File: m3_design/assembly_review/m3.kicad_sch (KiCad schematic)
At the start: 15 parts, among them J3 USB-C 2.0, U2 AP63203WU-7

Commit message: Validate and harden R5 flight computer CAD
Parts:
- C10, C11, C6, C7, C8, C9: Manufacturer (none) -> Samsung Electro-Mechanics; Manufacturer Part (none) -> CL21A226MAQNNNE
- C28: Manufacturer (none) -> Samsung Electro-Mechanics; Manufacturer Part (none) -> CL10A475KO8NNNC
- C5: Manufacturer (none) -> Samsung Electro-Mechanics; Manufacturer Part (none) -> CL05B104KO5NNNC
- D4: Manufacturer (none) -> STMicroelectronics; Manufacturer Part (none) -> USBLC6-2SC6
- J3: Manufacturer (none) -> Korean Hroparts Elec; Manufacturer Part (none) -> TYPE-C-31-M-12
- L1: Manufacturer (none) -> Sunlord; Manufacturer Part (none) -> SWPA4030S4R7MT
- R164: Manufacturer (none) -> UNI-ROYAL(Uniroyal Elec); Manufacturer Part (none) -> 0603WAF220KT5E
- R7, R8: Manufacturer (none) -> UNI-ROYAL(Uniroyal Elec); Manufacturer Part (none) -> 0402WGF5101TCE
- U2: Manufacturer (none) -> Diodes Incorporated; Manufacturer Part (none) -> AP63203WU-7
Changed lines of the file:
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@@
+				(font
+					(size 1.27 1.27))))
+		(property "Manufacturer" "Korean Hroparts Elec"
+			(at 63.5 76.2 0)
+			(hide yes)
+			(effects
+				(font
+					(size 1.27 1.27))))
+		(property "Manufacturer Part" "TYPE-C-31-M-12"
+			(at 63.5 76.2 0)
+			(hide yes)
+			(effects
 				(font
 					(size 1.27 1.27))))
@@
 				(font
 					(size 1.27 1.27))))
+		(property "Manufacturer" "STMicroelectronics"
+			(at 172.72 76.2 0)
+			(hide yes)
+			(effects
+				(font
+					(size 1.27 1.27))))
+		(property "Manufacturer Part" "USBLC6-2SC6"
+			(at 172.72 76.2 0)
+			(hide yes)
+			(effects
+				(font
+					(size 1.27 1.27))))
 		(instances
 			(project "m3"
@@
 				(font
 					(size 1.27 1.27))))
+		(property "Manufacturer" "Diodes Incorporated"
+			(at 284.48 76.2 0)
+			(hide yes)
+			(effects
+				(font
+					(size 1.27 1.27))))
+		(property "Manufacturer Part" "AP63203WU-7"
+			(at 284.48 76.2 0)
+			(hide yes)
+			(effects
+				(font
+					(size 1.27 1.27))))
 		(instances
 			(project "m3"
@@
 					(size 1.27 1.27))
 				(justify left)))
+		(property "Manufacturer" "Sunlord"
+			(at 261.62 154.94 0)
+			(hide yes)
+			(effects
+				(font
+					(size 1.27 1.27))
+				(justify left)))
+		(property "Manufacturer Part" "SWPA4030S4R7MT"
+			(at 261.62 154.94 0)
+			(hide yes)
+			(effects
+				(font
+					(size 1.27 1.27))
+				(justify left)))
 		(instances
 			(project "m3"
@@
 					(size 1.27 1.27))
 				(justify left)))
+		(property "Manufacturer" "UNI-ROYAL(Uniroyal Elec)"
+			(at 261.62 198.12 0)
+			(hide yes)
+			(effects
+				(font
+					(size 1.27 1.27))
+				(justify left)))
+		(property "Manufacturer Part" "0603WAF220KT5E"
+			(at 261.62 198.12 0)
+			(hide yes)
+			(effects
+				(font
+					(size 1.27 1.27))
+				(justify left)))
 		(instances
 			(project "m3"
@@
 					(size 1.27 1.27))
 				(justify left)))
+		(property "Manufacturer" "UNI-ROYAL(Uniroyal Elec)"
+			(at 40.64 116.84 0)
+			(hide yes)
+			(effects
+				(font
+					(size 1.27 1.27))
+				(justify left)))
+		(property "Manufacturer Part" "0402WGF5101TCE"
+			(at 40.64 116.84 0)
+			(hide yes)
+			(effects
+				(font
+					(size 1.27 1.27))
+				(justify left)))
 		(instances
 			(project "m3"
@@
 					(size 1.27 1.27))
 				(justify left)))
+		(property "Manufacturer" "UNI-ROYAL(Uniroyal Elec)"
+			(at 86.36 116.84 0)
+			(hide yes)
+			(effects
+				(font
+					(size 1.27 1.27))
+				(justify left)))
+		(property "Manufacturer Part" "0402WGF5101TCE"
+			(at 86.36 116.84 0)
+			(hide yes)
+			(effects
+				(font
+					(size 1.27 1.27))
+				(justify left)))
 		(instances
 			(project "m3"
@@
 					(size 1.27 1.27))
 				(justify left)))
+		(property "Manufacturer" "Samsung Electro-Mechanics"
+			(at 248.92 114.3 0)
+			(hide yes)
+			(effects
+				(font
+					(size 1.27 1.27))
+				(justify left)))
+		(property "Manufacturer Part" "CL05B104KO5NNNC"
+			(at 248.92 114.3 0)
+			(hide yes)
+			(effects
+				(font
+					(size 1.27 1.27))
+				(justify left)))
 		(instances
 			(project "m3"
@@
 					(size 1.27 1.27))
 				(justify left)))
+		(property "Manufacturer" "Samsung Electro-Mechanics"
+			(at 279.4 114.3 0)
+			(hide yes)
+			(effects
+				(font
+					(size 1.27 1.27))
+				(justify left)))
+		(property "Manufacturer Part" "CL21A226MAQNNNE"
+			(at 279.4 114.3 0)
+			(hide yes)
+			(effects
+				(font
+					(size 1.27 1.27))
+				(justify left)))
 		(instances
 			(project "m3"
@@
 					(size 1.27 1.27))
 				(justify left)))
+		(property "Manufacturer" "Samsung Electro-Mechanics"
+			(at 309.88 114.3 0)
+			(hide yes)
+			(effects
+				(font
+					(size 1.27 1.27))
+				(justify left)))
+		(property "Manufacturer Part" "CL21A226MAQNNNE"
+			(at 309.88 114.3 0)
+			(hide yes)
+			(effects
+				(font
+					(size 1.27 1.27))
+				(justify left)))
 		(instances
 			(project "m3"
@@
 					(size 1.27 1.27))
 				(justify left)))
+		(property "Manufacturer" "Samsung Electro-Mechanics"
+			(at 294.64 154.94 0)
+			(hide yes)
+			(effects
+				(font
+					(size 1.27 1.27))
+				(justify left)))
+		(property "Manufacturer Part" "CL21A226MAQNNNE"
+			(at 294.64 154.94 0)
+			(hide yes)
+			(effects
+				(font
+					(size 1.27 1.27))
+				(justify left)))
 		(instances
 			(project "m3"
@@
 					(size 1.27 1.27))
 				(justify left)))
+		(property "Manufacturer" "Samsung Electro-Mechanics"
+			(at 327.66 154.94 0)
+			(hide yes)
+			(effects
+				(font
+					(size 1.27 1.27))
+				(justify left)))
+		(property "Manufacturer Part" "CL21A226MAQNNNE"
+			(at 327.66 154.94 0)
+			(hide yes)
+			(effects
+				(font
+					(size 1.27 1.27))
+				(justify left)))
 		(instances
 			(project "m3"
@@
 					(size 1.27 1.27))
 				(justify left)))
+		(property "Manufacturer" "Samsung Electro-Mechanics"
+			(at 294.64 198.12 0)
+			(hide yes)
+			(effects
+				(font
+					(size 1.27 1.27))
+				(justify left)))
+		(property "Manufacturer Part" "CL21A226MAQNNNE"
+			(at 294.64 198.12 0)
+			(hide yes)
+			(effects
+				(font
+					(size 1.27 1.27))
+				(justify left)))
 		(instances
 			(project "m3"
@@
 					(size 1.27 1.27))
 				(justify left)))
+		(property "Manufacturer" "Samsung Electro-Mechanics"
+			(at 327.66 198.12 0)
+			(hide yes)
+			(effects
+				(font
+					(size 1.27 1.27))
+				(justify left)))
+		(property "Manufacturer Part" "CL21A226MAQNNNE"
+			(at 327.66 198.12 0)
+			(hide yes)
+			(effects
+				(font
+					(size 1.27 1.27))
+				(justify left)))
 		(instances
 			(project "m3"
@@
 			(at 63.5 144.78 0)
 			(hide yes)
+			(effects
+				(font
+					(size 1.27 1.27))
+				(justify left)))
+		(property "Manufacturer" "Samsung Electro-Mechanics"
+			(at 63.5 144.78 0)
+			(hide yes)
+			(effects
+				(font
+					(size 1.27 1.27))
+				(justify left)))
+		(property "Manufacturer Part" "CL10A475KO8NNNC"
+			(at 63.5 144.78 0)
+			(hide yes)

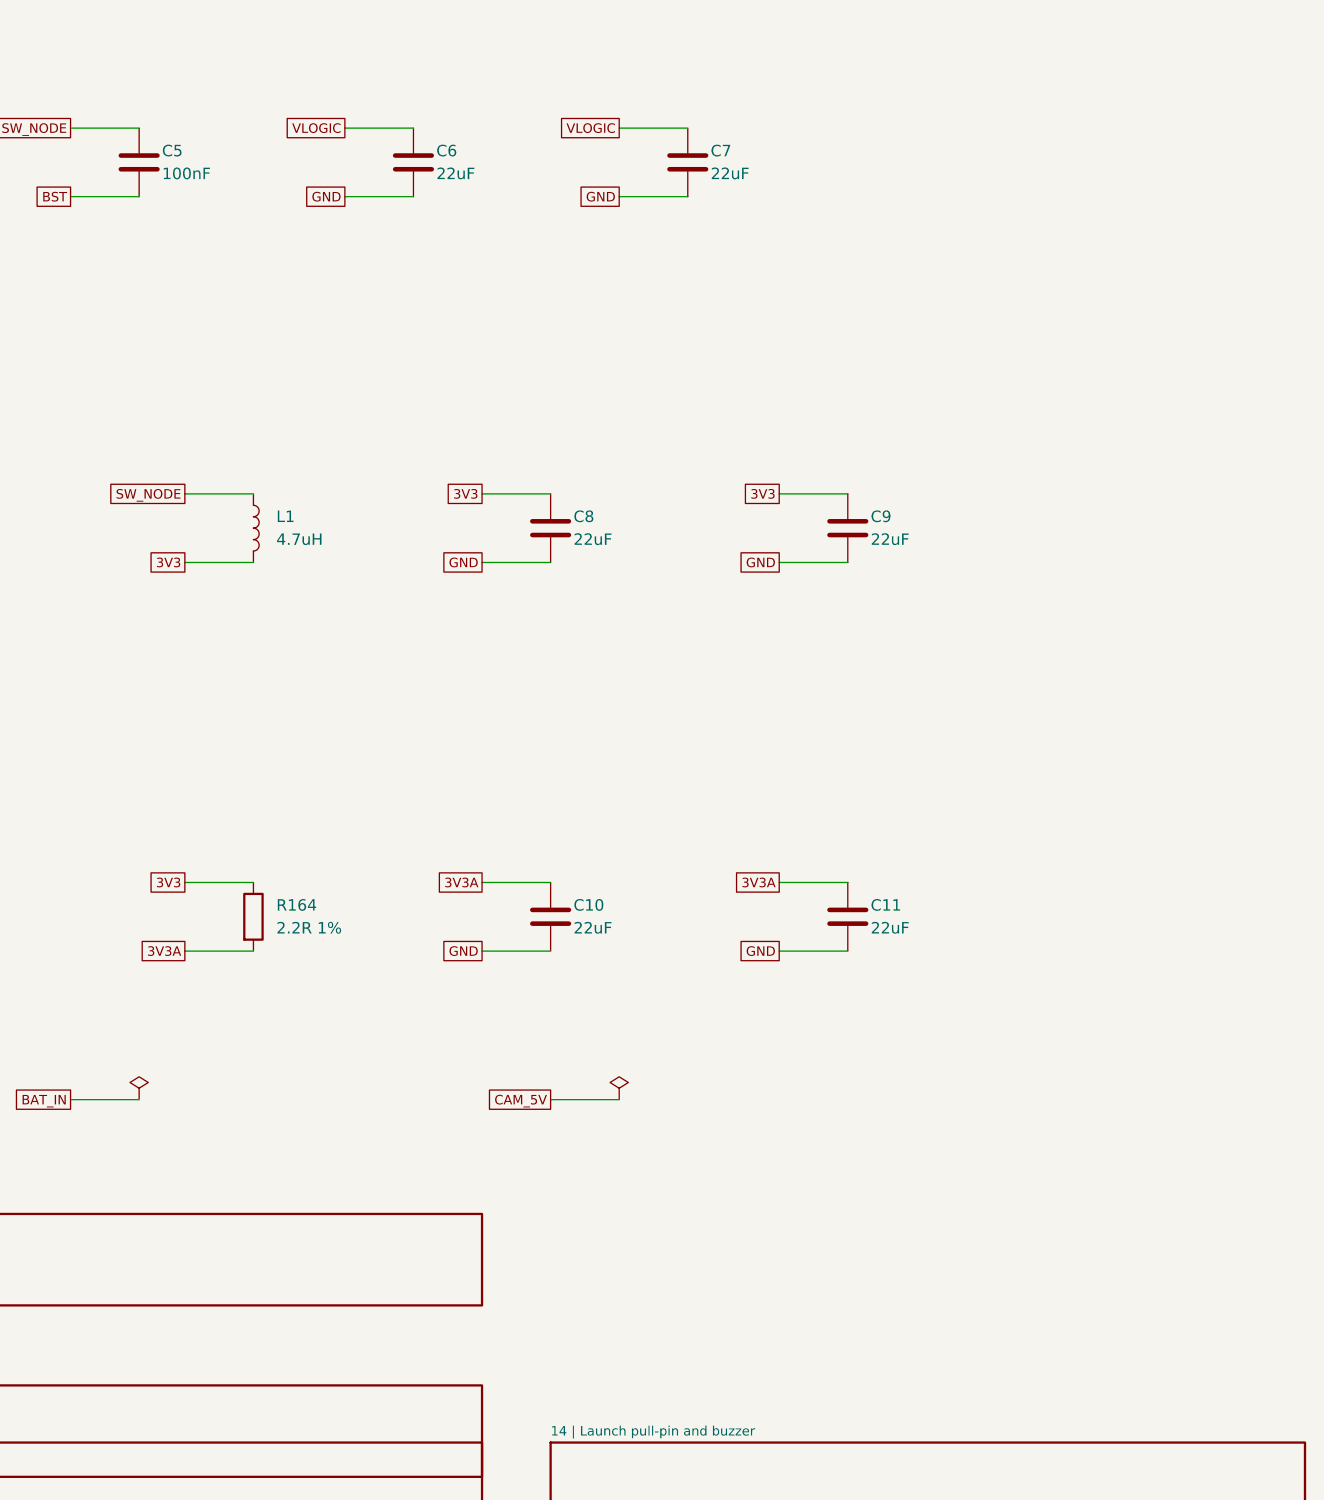
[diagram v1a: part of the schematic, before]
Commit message: Complete R6 flight computer CAD and validated fabrication package
Add protected radio and GPS ports, reset-off port power, compact connectors and single-channel pyro layout. Close independent routing, ground-return and decoupling findings; record zero-error CAD checks and current manufacturing artifacts. Document 100 mm length, IMU stock hold and remaining firmware and hardware qualification.
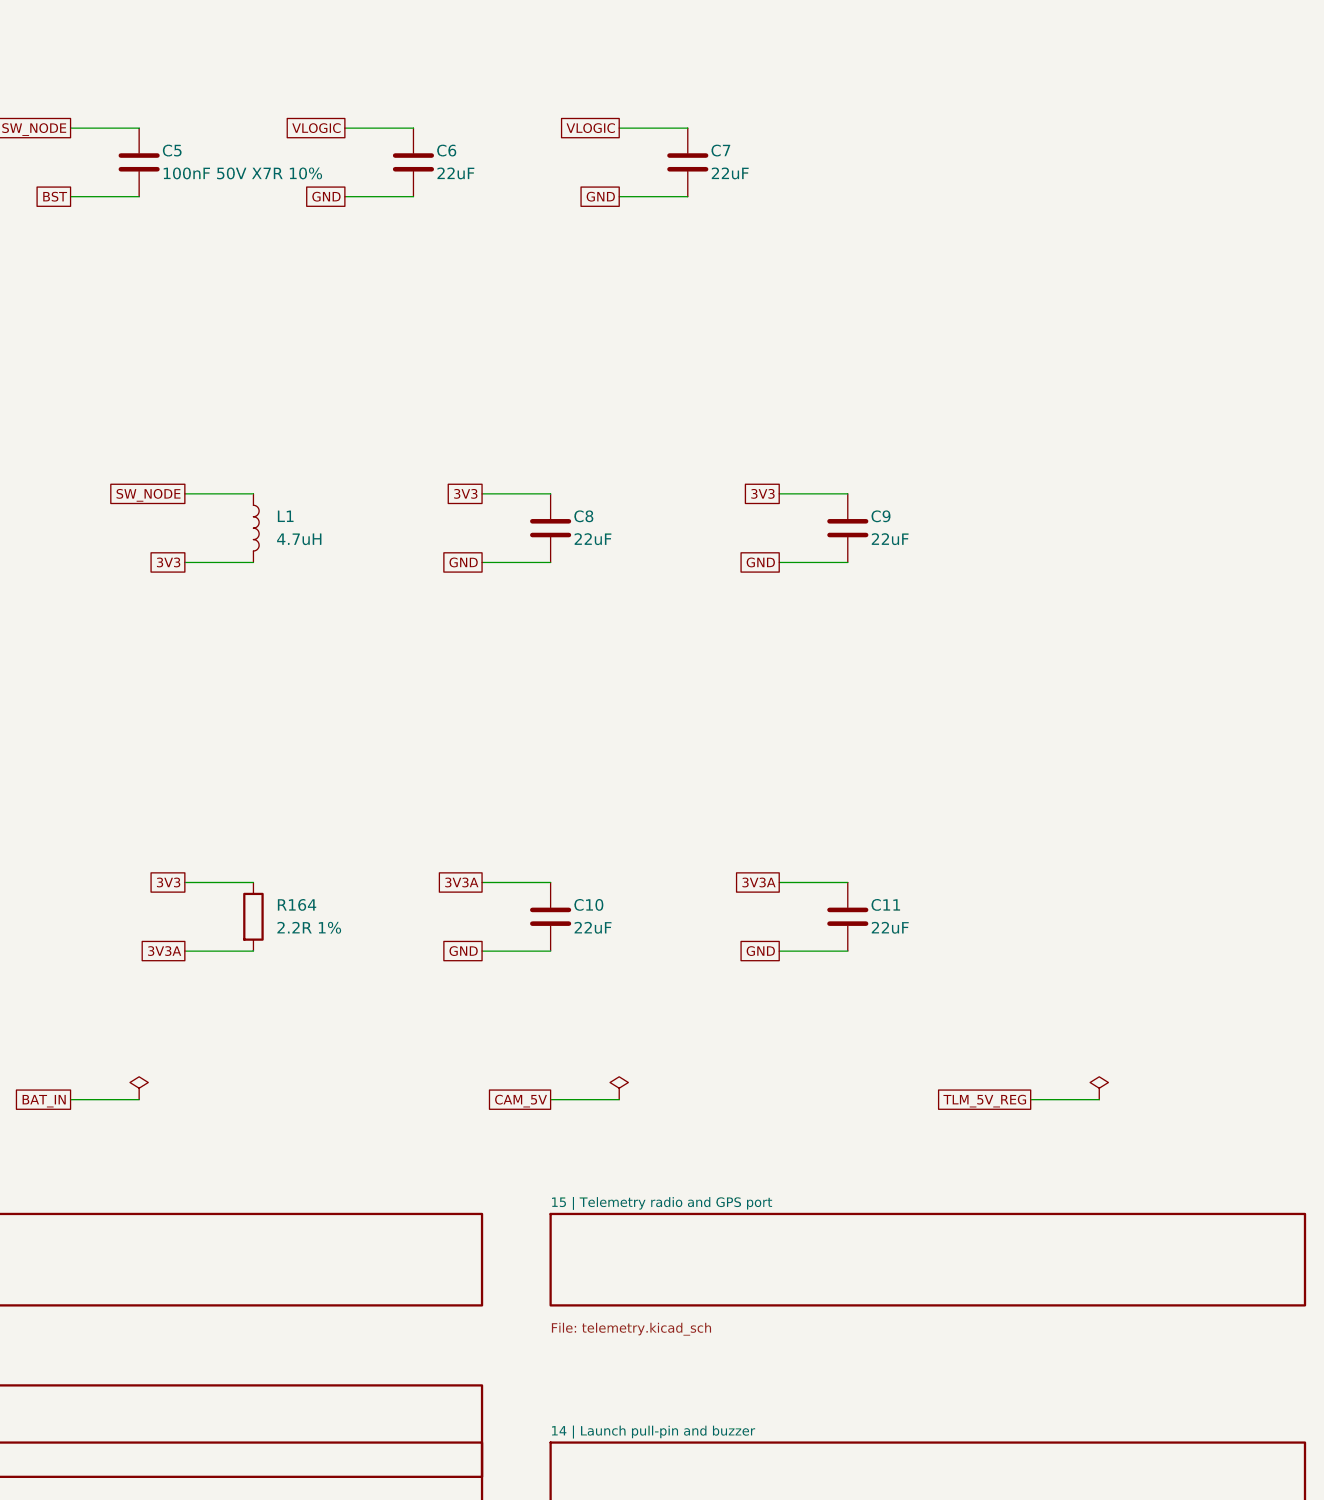
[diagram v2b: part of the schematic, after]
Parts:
- C5: value 100nF -> 100nF 50V X7R 10%; LCSC C1525 -> C307331; LCSC Part (none) -> C307331; Manufacturer Part CL05B104KO5NNNC -> CL05B104KB54PNC
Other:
- added sheet 15 | Telemetry radio and GPS port (telemetry.kicad_sch)
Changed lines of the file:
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@@
 		(title "01 | USB input and regulated supplies")
 		(date "2026-09-07")
-		(rev "M3-ASSY-R4")
+		(rev "M3-ASSY-R6")
 		(company "Single-board M3 candidate; full system incomplete"))
 	(text "01 | USB input and regulated supplies"
@@
 					(size 1.27 1.27))
 				(justify left)))
-		(property "Value" "100nF"
+		(property "Value" "100nF 50V X7R 10%"
 			(at 251.45999999999998 115.57000000000001 0)
 			(effects
@@
 					(size 1.27 1.27))
 				(justify left)))
-		(property "LCSC" "C1525"
+		(property "LCSC" "C307331"
 			(at 248.92 114.3 0)
 			(hide yes)
@@
 					(size 1.27 1.27))
 				(justify left)))
-		(property "Manufacturer Part" "CL05B104KO5NNNC"
+		(property "Manufacturer Part" "CL05B104KB54PNC"
 			(at 248.92 114.3 0)
 			(hide yes)
@@
 				(path "/6007a7db-6a58-5660-8beb-956dea045ff8"
 					(reference "C5")
-					(unit 1)))))
+					(unit 1))))		(property "LCSC Part" "C307331"
+			(at 0 0 0)
+			(hide yes)
+			(effects
+				(font
+					(size 1.27 1.27))
+				(justify left)))
+)
 	(wire
 		(pts
@@
 			(justify right))
 )
+	(symbol
+		(lib_id "M3:PWR_FLAG")
+		(at 355.6 218.44 0)
+		(unit 1)
+		(in_bom no)
+		(on_board no)
+		(dnp no)
+		(property "Reference" "#FLG07"
+			(at 355.6 210.82 0)
+			(hide yes)
+			(effects
+				(font
+					(size 1.27 1.27))))
+		(property "Value" "PWR_FLAG"
+			(at 355.6 214.63 0)
+			(hide yes)
+			(effects
+				(font
+					(size 1.27 1.27))))
+		(property "Footprint" ""
+			(at 355.6 218.44 0)
+			(hide yes)
+			(effects
+				(font
+					(size 1.27 1.27))))
+		(property "Datasheet" ""
+			(at 355.6 218.44 0)
+			(hide yes)
+			(effects
+				(font
+					(size 1.27 1.27))))
+		(property "LCSC" ""
+			(at 355.6 218.44 0)
+			(hide yes)
+			(effects
+				(font
+					(size 1.27 1.27))))
+		(instances
+			(project "m3"
+				(path "/6007a7db-6a58-5660-8beb-956dea045ff8"
+					(reference "#FLG07")
+					(unit 1)))))
+	(wire
+		(pts
+			(xy 355.6 218.44)
+			(xy 347.98 218.44))
+		(stroke
+			(width 0)
+			(type default))
+)
+	(global_label "TLM_5V_REG"
+		(shape passive)
+		(at 347.98 218.44 0)
+		(effects
+			(font
+				(size 1.05 1.05))
+			(justify right))
+)
 	(sheet
 		(at 20.32 231.14)
@@
 				(path "/6007a7db-6a58-5660-8beb-956dea045ff8"
 					(page "14")))))
+	(sheet
+		(at 294.64 231.14)
+		(size 83.82 10.16)
+		(stroke
+			(width .254)
+			(type default))
+		(fill
+			(color 0 0 0 0))
+		(property "Sheetname" "15 | Telemetry radio and GPS port"
+			(at 294.64 229.87 0)
+			(effects
+				(font
+					(size 1.05 1.05))
+				(justify left)))
+		(property "Sheetfile" "telemetry.kicad_sch"
+			(at 294.64 243.84 0)
+			(effects
+				(font
+					(size 1.05 1.05))
+				(justify left)))
+		(instances
+			(project "m3"
+				(path "/6007a7db-6a58-5660-8beb-956dea045ff8"
+					(page "15")))))
 	(sheet_instances
 		(path "/"
